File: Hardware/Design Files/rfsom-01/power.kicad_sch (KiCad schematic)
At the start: 44 parts, among them U1 TPS62086RLT, U12 TPS51200DRCR, U2 TPS51200DRCR, U3 LP8758A1E0YFFR

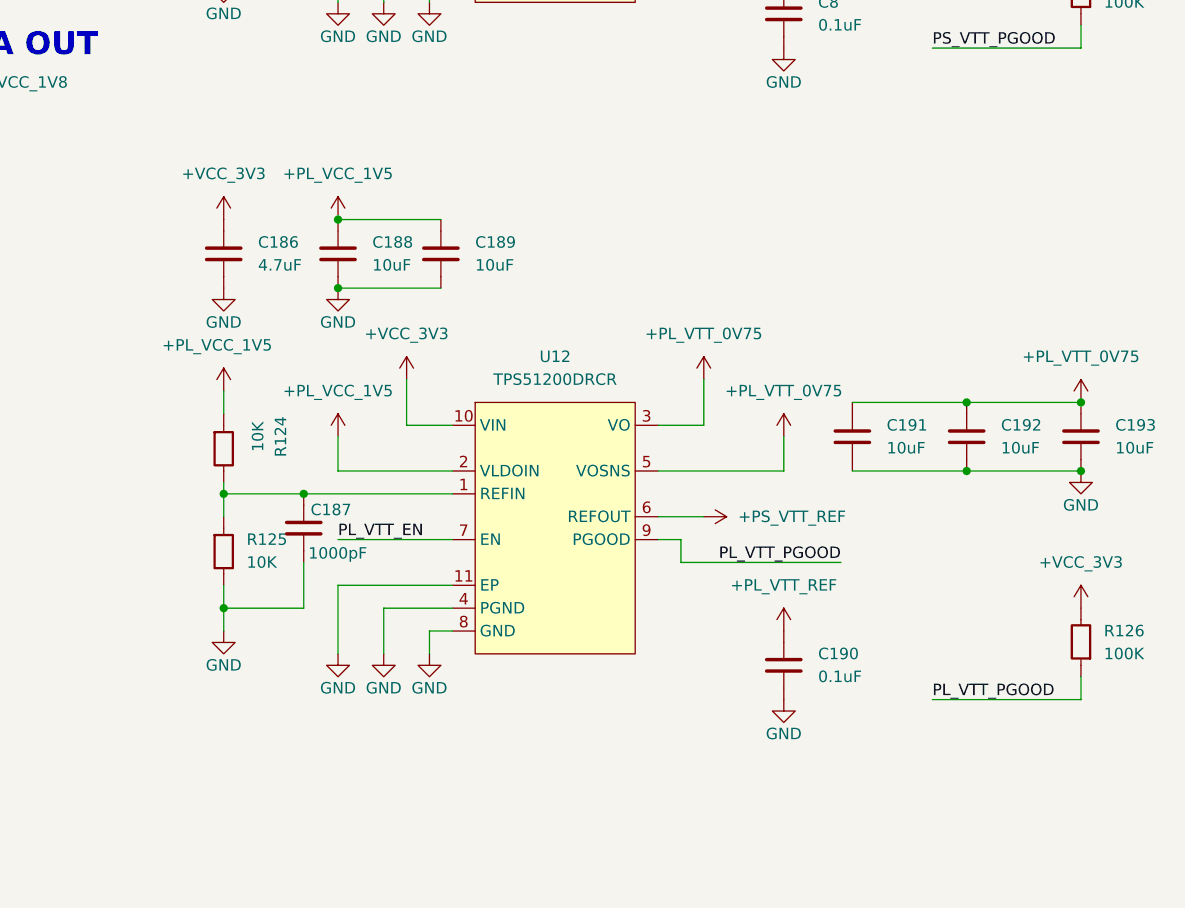
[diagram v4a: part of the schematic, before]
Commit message: routing changes; added mezzanine; added pl ram;
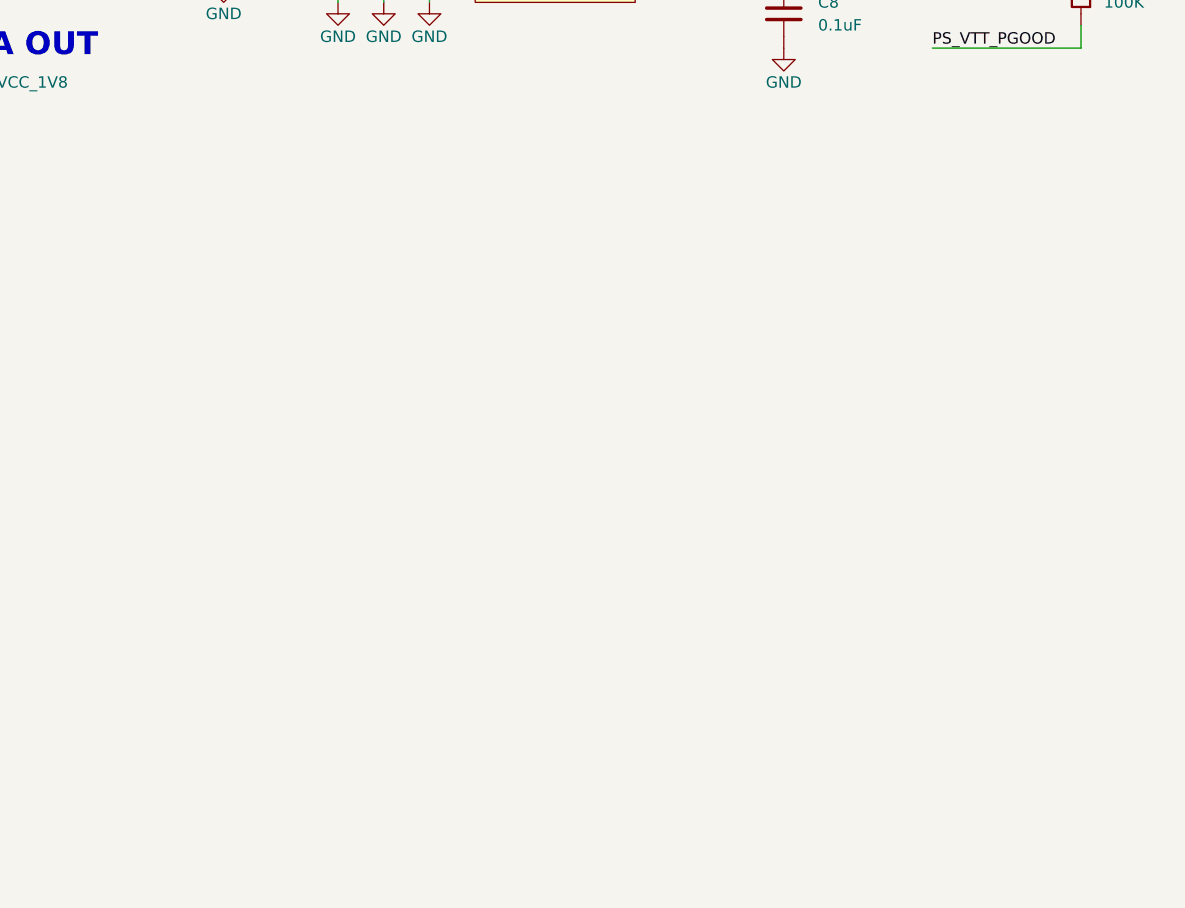
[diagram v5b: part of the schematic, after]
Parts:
- removed C186: CL21B475KPFNNNE, Capacitor_SMD:C_0805_2012Metric, symbol Capacitors:CL21B475KPFNNNE
- removed C187: CL05B102KB5NNNC, Capacitor_SMD:C_0402_1005Metric, symbol Capacitors:CL05B102KB5NNNC
- removed C188, C189, C191, C192, C193: CL21B106KQQNFNE, Capacitor_SMD:C_0805_2012Metric, symbol Capacitors:CL21B106KQQNFNE
- removed C190: CL05B104KA5NNNC, Capacitor_SMD:C_0402_1005Metric, symbol Capacitors:CL05B104KA5NNNC
- removed R124, R125: RC0603FR-0710KL, Resistor_SMD:R_0603_1608Metric, symbol Resistors:RC0603FR-0710KL
- removed R126: RC0402FR-07100KL, Resistor_SMD:R_0402_1005Metric, symbol Resistors:RC0402FR-07100KL
- removed U12: TPS51200DRCR, Package_SON:VSON-10-1EP_3x3mm_P0.5mm_EP1.65x2.4mm, symbol ICs:TPS51200DRCR

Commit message: updated sch pdf; routign progress;
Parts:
- added C10, C11, C8, C9: CL31A106KBHNNNE, Capacitor_SMD:C_1206_3216Metric_Pad1.33x1.80mm_HandSolder, symbol Capacitors:CL31A106KBHNNNE
- added C12, C13, C14, C15: CL21B475KPFNNNE, Capacitor_SMD:C_0805_2012Metric, symbol Capacitors:CL21B475KPFNNNE
- added C212, C213, C214, C215: CL10B104KB8NNWC, Capacitor_SMD:C_0603_1608Metric_Pad1.08x0.95mm_HandSolder, symbol Capacitors:CL10B104KB8NNWC
- renumbered C12 to C2, C3 to C216, C6 to C217, C4 to C218, C5 to C219, C8 to C220, C9 to C221, C10 to C222, C11 to C223, C13 to C3, C14 to C4, C15 to C5, C2 to C6, R3 to R1, R1 to R10, R2 to R11, R5 to R12, R4 to R2, R8 to R3, R9 to R4, R10 to R5, R11 to R8, R12 to R9, U3 to U2, U2 to U3
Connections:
- net +PS_VCC_1V5: now also C13.1, C213.1, C9.1
- net +VCC_1V0: now also C12.1, C212.1, C8.1
- net +VCC_1V2: now also C10.1, C14.1, C214.1
- net +VCC_1V8: now also C11.1, C15.1, C215.1
- net GND: now also C10.2, C11.2, C12.2, C13.2, C14.2, C15.2, C212.2, C213.2, C214.2, C215.2, C8.2, C9.2

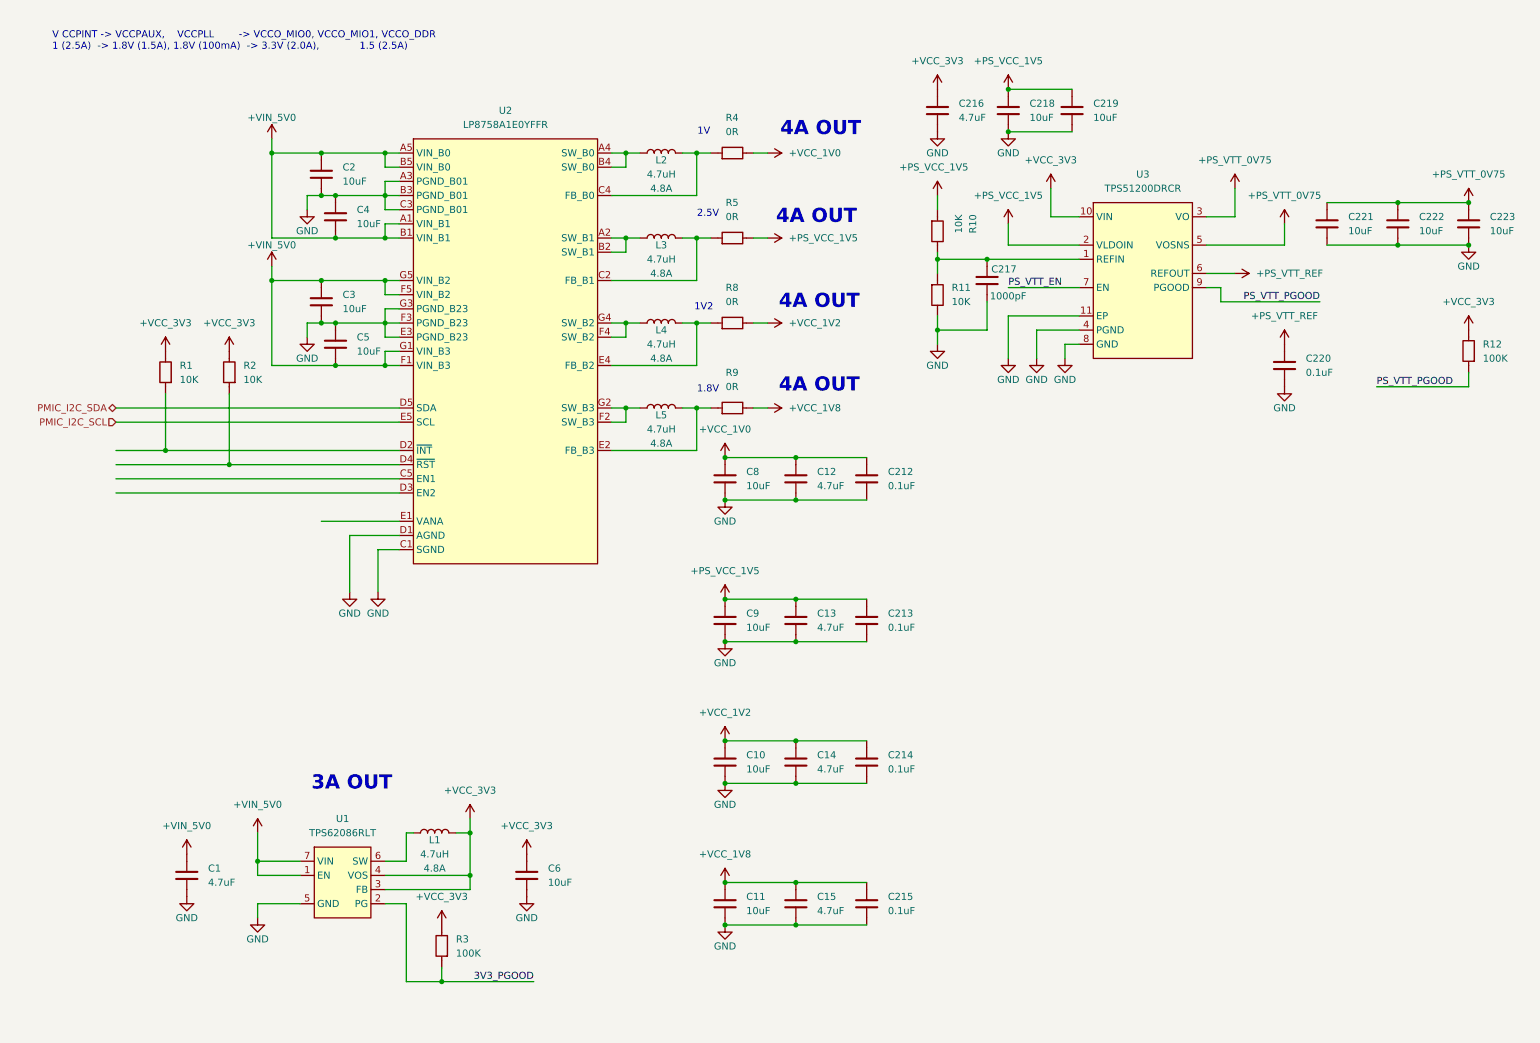
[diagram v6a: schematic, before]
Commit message: replaced pmic;
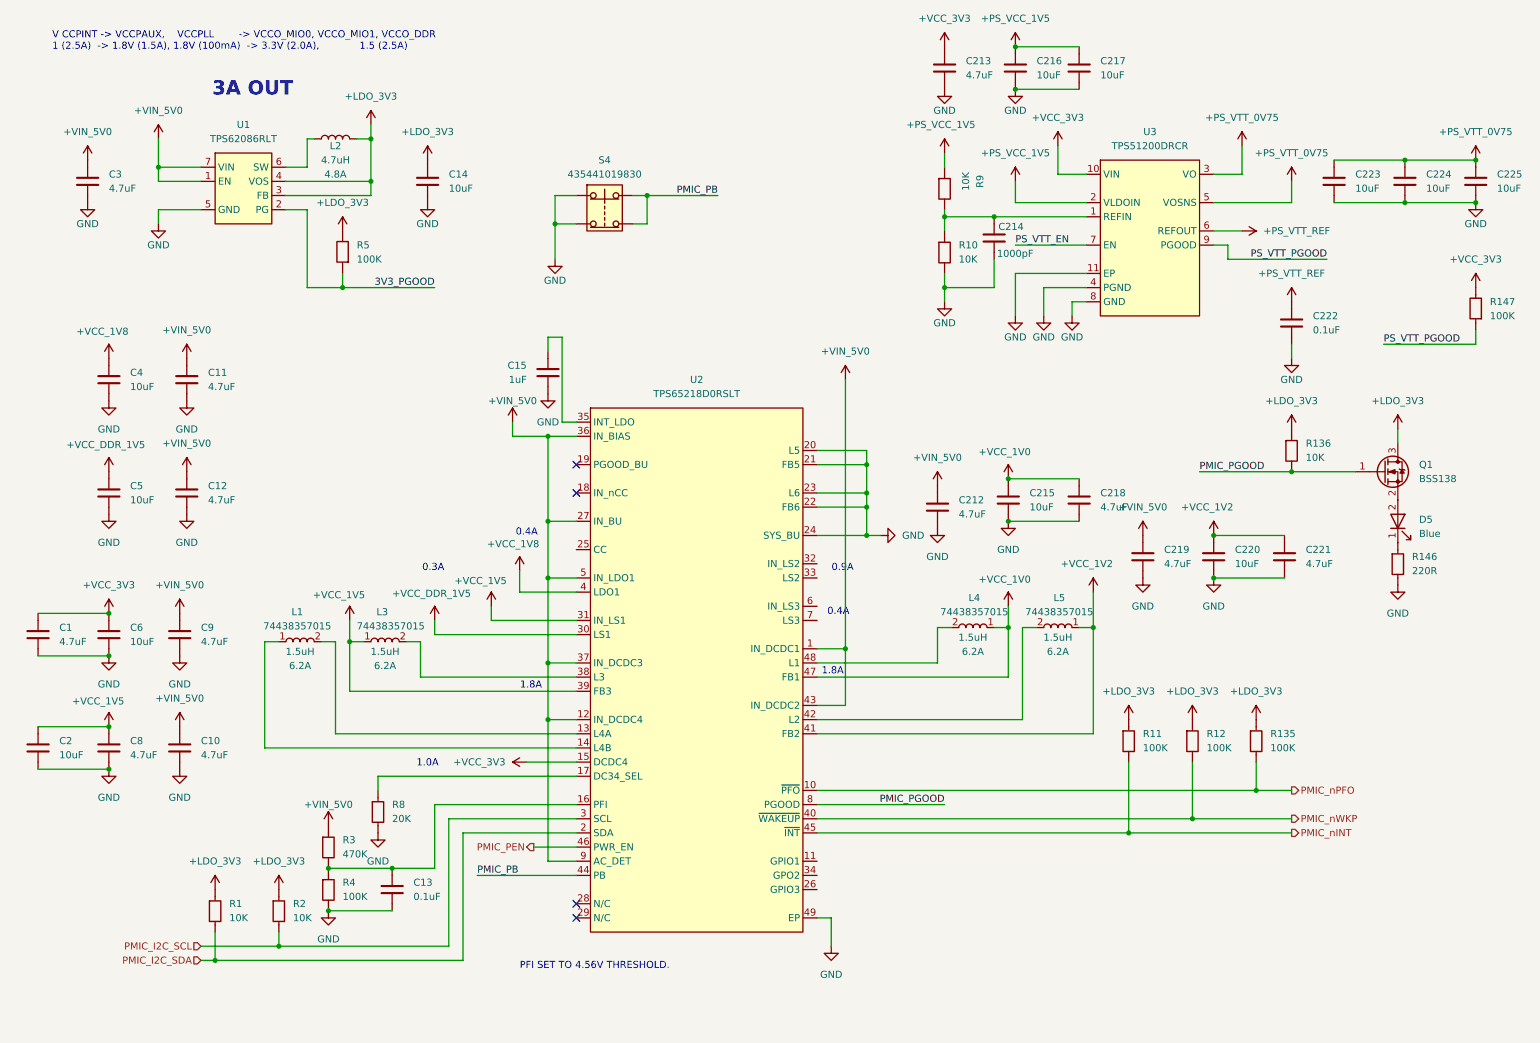
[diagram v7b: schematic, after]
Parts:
- removed C10, C11, C8, C9: CL31A106KBHNNNE, Capacitor_SMD:C_1206_3216Metric_Pad1.33x1.80mm_HandSolder, symbol Capacitors:CL31A106KBHNNNE
- removed C13, C14, C15: CL21B475KPFNNNE, Capacitor_SMD:C_0805_2012Metric, symbol Capacitors:CL21B475KPFNNNE
- removed C2, C3, C4, C5: CL31A106KBHNNNE, Capacitor_SMD:C_1206_3216Metric, symbol Capacitors:CL31A106KBHNNNE
- removed C212, C213, C214, C215: CL10B104KB8NNWC, Capacitor_SMD:C_0603_1608Metric_Pad1.08x0.95mm_HandSolder, symbol Capacitors:CL10B104KB8NNWC
- removed L2, L3, L4, L5: DFE322512F-R47M=P2, Inductors:IND_1210, symbol Inductors:DFE322512F-R47M=P2
- removed R4, R5, R8, R9: RC0603JR-070RL, Resistor_SMD:R_0603_1608Metric, symbol Resistors:RC0603JR-070RL
- removed U2: LP8758A1E0YFFR, ICs:R-XBGA-N35, symbol ICs:LP8758A1E0YFFR
- added C1, C10, C11, C212, C218, C219, C221, C8, C9: CL21B475KPFNNNE, Capacitor_SMD:C_0805_2012Metric, symbol Capacitors:CL21B475KPFNNNE
- added C13: CL05B104KA5NNNC, Capacitor_SMD:C_0402_1005Metric, symbol Capacitors:CL05B104KA5NNNC
- added C15: CL10B105KA8NNNC, Capacitor_SMD:C_0603_1608Metric, symbol Capacitors:CL10B105KA8NNNC
- added C2, C215, C220, C4, C5, C6: CL21B106KQQNFNE, Capacitor_SMD:C_0805_2012Metric, symbol Capacitors:CL21B106KQQNFNE
- added D5: 150060BS75000, LED_SMD:LED_0603_1608Metric, symbol Diodes:150060BS75000
- added L1, L3, L4, L5: 74438357015, Inductors:WE-MAPI, symbol Inductors:74438357015
- added Q1: BSS138, Package_TO_SOT_SMD:SOT-23, symbol Transistor_FET:BSS138
- added R11, R12, R135, R4: RC0402FR-07100KL, Resistor_SMD:R_0402_1005Metric, symbol Resistors:RC0402FR-07100KL
- added R136: RC0603FR-0710KL, Resistor_SMD:R_0603_1608Metric, symbol Resistors:RC0603FR-0710KL
- added R146: RC0603FR-07220RL, Resistor_SMD:R_0603_1608Metric, symbol Resistors:RC0603FR-07220RL
- added R3: RC0402FR-13470KL, Resistor_SMD:R_0402_1005Metric, symbol Resistors:RC0402FR-13470KL
- added R8: RC0603FR-0720KL, Resistor_SMD:R_0201_0603Metric, symbol Resistors:RC0603FR-0720KL
- added S4: 435441019830, Miscellaneous:435441019830, symbol Miscellaneous:435441019830
- added U2: TPS65218D0RSLT, ICs:RSL0048G, symbol ICs:TPS65218D0RSLT
- renumbered C6 to C14, C216 to C213, C217 to C214, C218 to C216, C219 to C217, C220 to C222, C221 to C223, C222 to C224, C223 to C225, C1 to C3, L1 to L2, R11 to R10, R12 to R147, R3 to R5, R10 to R9
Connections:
- net +VCC_1V0: now also C215.1, C218.1, L4.1, U2.47 (FB1); no longer C12.1
- net +VCC_1V2: now also C220.1, C221.1, L5.1, U2.41 (FB2)
- net +VCC_1V8: now also C4.1, U2.4 (LDO1)
- net +VCC_3V3: now also C1.1, C6.1, U2.15 (DCDC4); no longer C14.1, L2.2, R1.2, R2.2, R5.2, U1.3 (FB), U1.4 (VOS)
- net +VIN_5V0: now also C12.1, C10.1, C11.1, C212.1, C219.1, C9.1, R3.1, U2.1 (IN_DCDC1), U2.12 (IN_DCDC4), U2.27 (IN_BU), U2.36 (IN_BIAS), U2.37 (IN_DCDC3), U2.43 (IN_DCDC2), U2.5 (IN_LDO1), U2.9 (AC_DET)
- net GND: now also C1.2, C10.2, C11.2, C13.2, C15.2, C2.2, C212.2, C215.2, C218.2, C219.2, C220.2, C221.2, C4.2, C5.2, C6.2, C8.2, C9.2, R146.2, R4.2, R8.2, S4.1, S4.3, U2.20 (L5), U2.21 (FB5), U2.22 (FB6), U2.23 (L6), U2.24 (SYS_BU), U2.49 (EP)
- net PMIC_I2C_SCL: now also R2.2, U2.3 (SCL)
- net PMIC_I2C_SDA: now also R1.2, U2.2 (SDA)
- net +LDO_3V3: now reaches R2.1
- net +LDO_3V3: now also C14.1, L2.2, R1.1, R5.2, U1.3 (FB), U1.4 (VOS), Q1.3 (D), R11.1, R12.1, R135.1, R136.1
- new net: C15.1, U2.35 (INT_LDO)
- new net: C13.1, R3.2, R4.1, U2.16 (PFI)
- new net: R8.1, U2.17 (DC34_SEL)
- new net: D5.1 (K), R146.1
- new net: L1.2, U2.13 (L4A)
- new net: L1.1, U2.14 (L4B)
- new net: L3.2, U2.38 (L3)
- new net: L5.2, U2.42 (L2)
- new net: L4.2, U2.48 (L1)
- new net: D5.2 (A), Q1.2 (S)
- new net +VCC_1V5: C2.1, C8.1, L3.1, U2.31 (IN_LS1), U2.39 (FB3)
- new net +VCC_DDR_1V5: C5.1, U2.30 (LS1)
- new net PMIC_PB: S4.2, S4.4, U2.44 (PB)
- new net PMIC_PEN: U2.46 (PWR_EN)
- new net PMIC_PGOOD: Q1.1 (G), R136.2, U2.8 (PGOOD)
- new net PMIC_nINT: R11.2, U2.45 (~{INT})
- new net PMIC_nPFO: R135.2, U2.10 (~{PFO})
- new net PMIC_nWKP: R12.2, U2.40 (~{WAKEUP})
- no-connect marks 0 -> 4
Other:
- note added: "0.3A"
- note added: "0.4A"
- note added: "0.9A"
- note added: "1.0A"
- note added: "1.8A"
- note added: "PFI SET TO 4.56V THRESHOLD."
- note removed: "1.8V"
- note removed: "1V"
- note removed: "1V2"
- note removed: "2.5V"
- note removed: "4A OUT"
- moved on the sheet: C14, C213, C214, C216, C217, C222, C223, C224, C225, C3, L2, R10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
